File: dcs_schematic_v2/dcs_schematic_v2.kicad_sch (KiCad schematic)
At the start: 34 parts, among them J1 from_encoder, M1 Motor_DC, Q1 IRLZ44N, U1 OPA2197xD, U2 OPA2197xD, U3 OPA2197xD, U5 LM2917N-8_NOPB, U6 74HC86, U7 OPA2197xD, U8 LM311

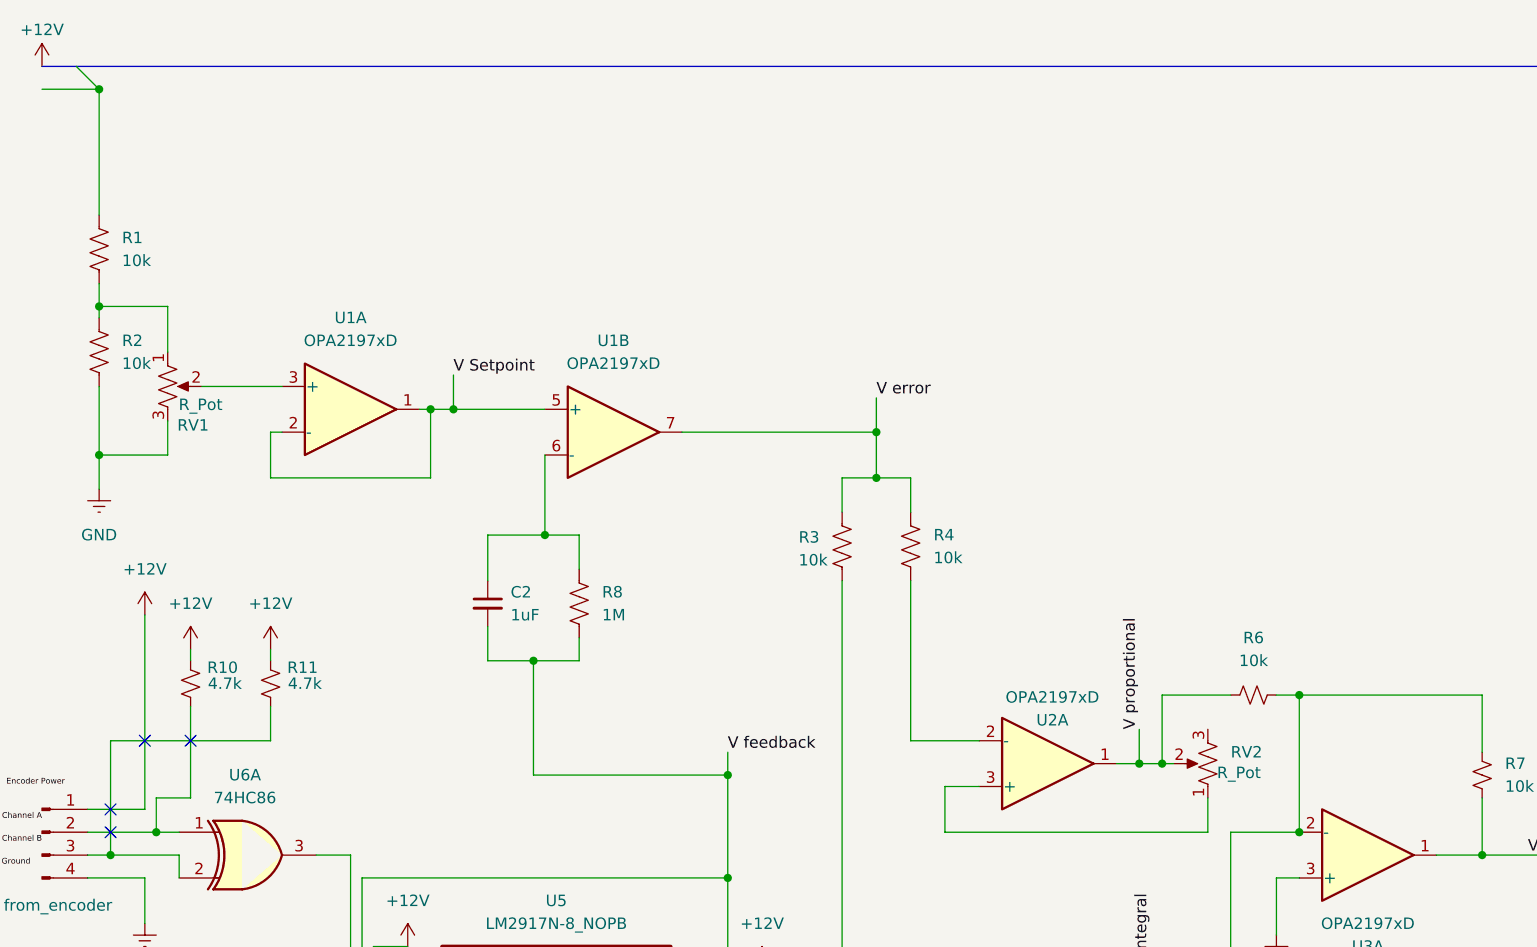
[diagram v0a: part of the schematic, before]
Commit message: added power supplies for op-amps. will need to download correct models and update schematic
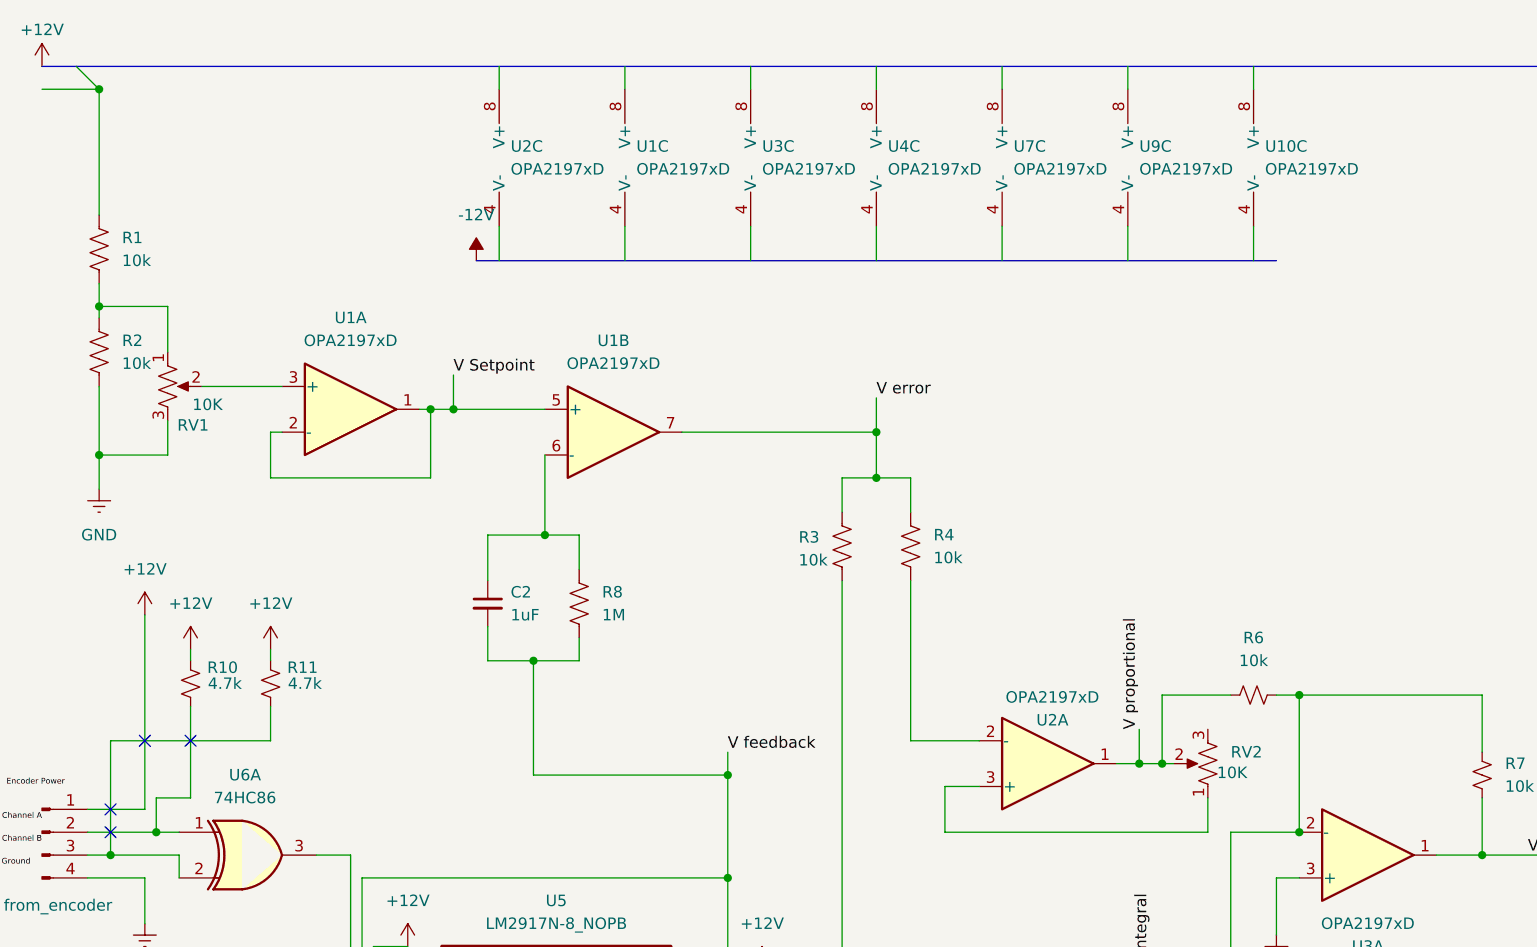
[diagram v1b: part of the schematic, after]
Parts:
- added unit 3 of U1
- added U10, U4, U9: OPA2197xD, Package_SO:SOIC-8_3.9x4.9mm_P1.27mm, symbol Amplifier_Operational:OPA2197xD
- added unit 3 of U2
- added unit 3 of U3
- added unit 3 of U7
- RV1, RV2: value R_Pot -> 10K
